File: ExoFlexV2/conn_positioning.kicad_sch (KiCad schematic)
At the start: 39 parts

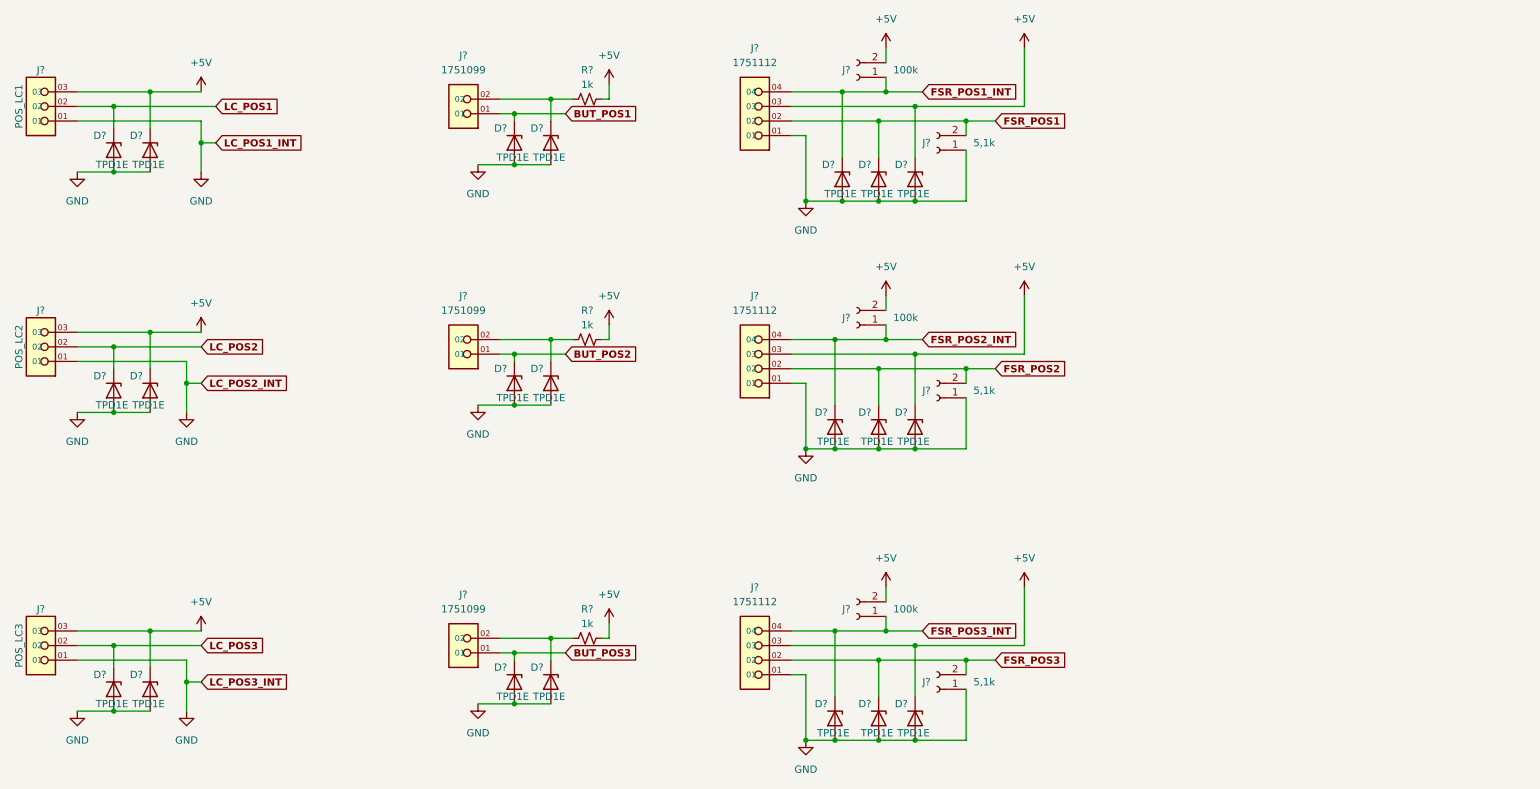
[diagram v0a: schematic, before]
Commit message: Mise à jour signaux STM
- Condo de découplage
- Signaux supplémentaire pour le STM
- Page GND sera pour Multiplexeur
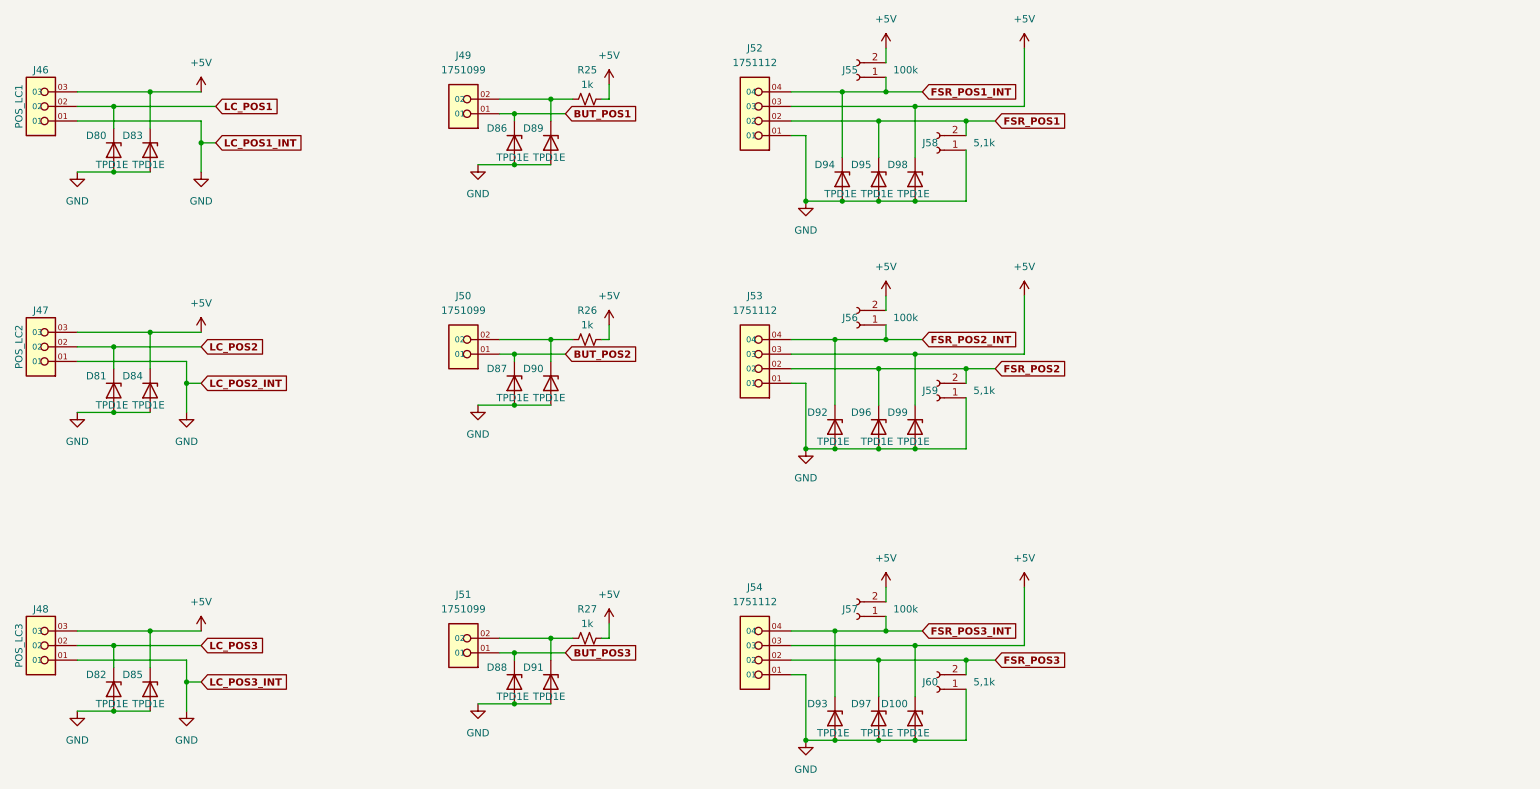
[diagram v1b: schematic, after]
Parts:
- gave numbers to parts that had none: 39

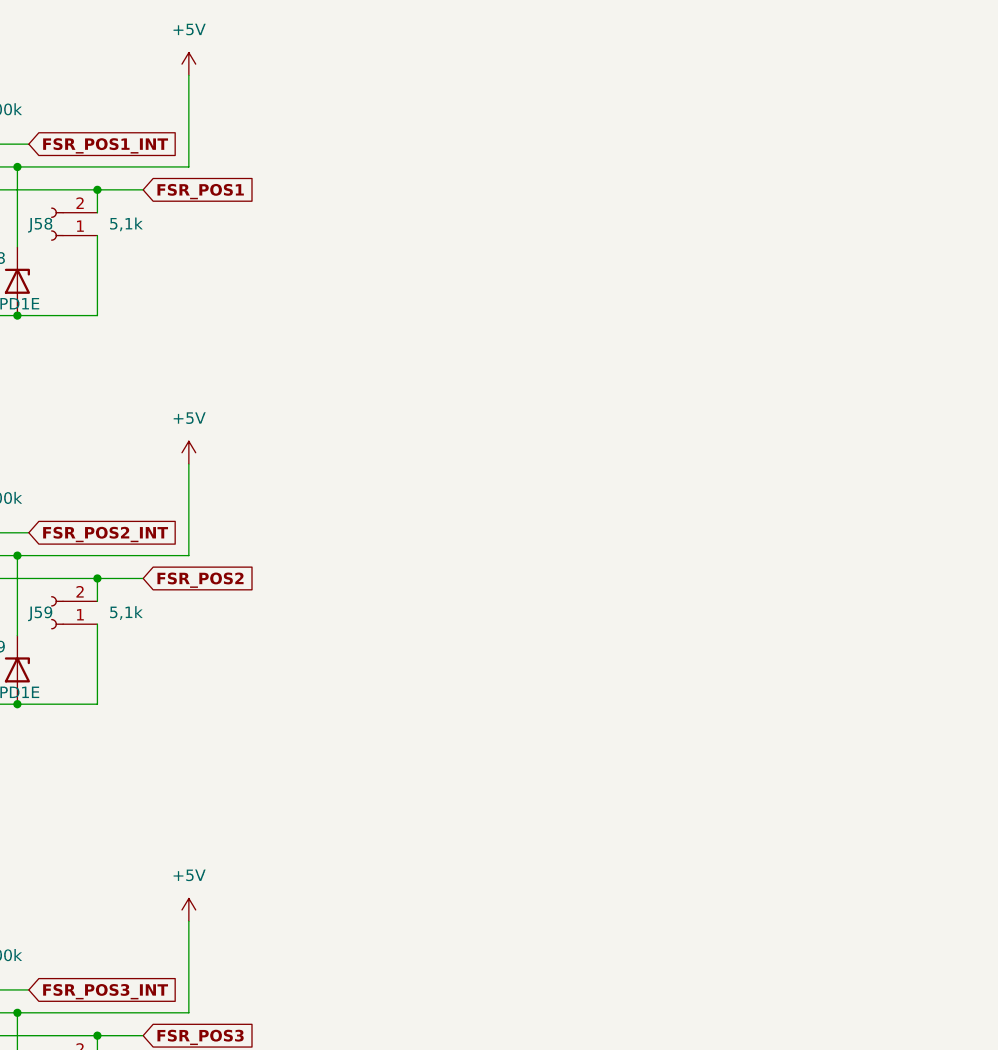
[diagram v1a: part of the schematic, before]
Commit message: Finalisation 1
- Ajout de pages pour la gestion des signaux négatif
- Modification des pages de torque et amplitude
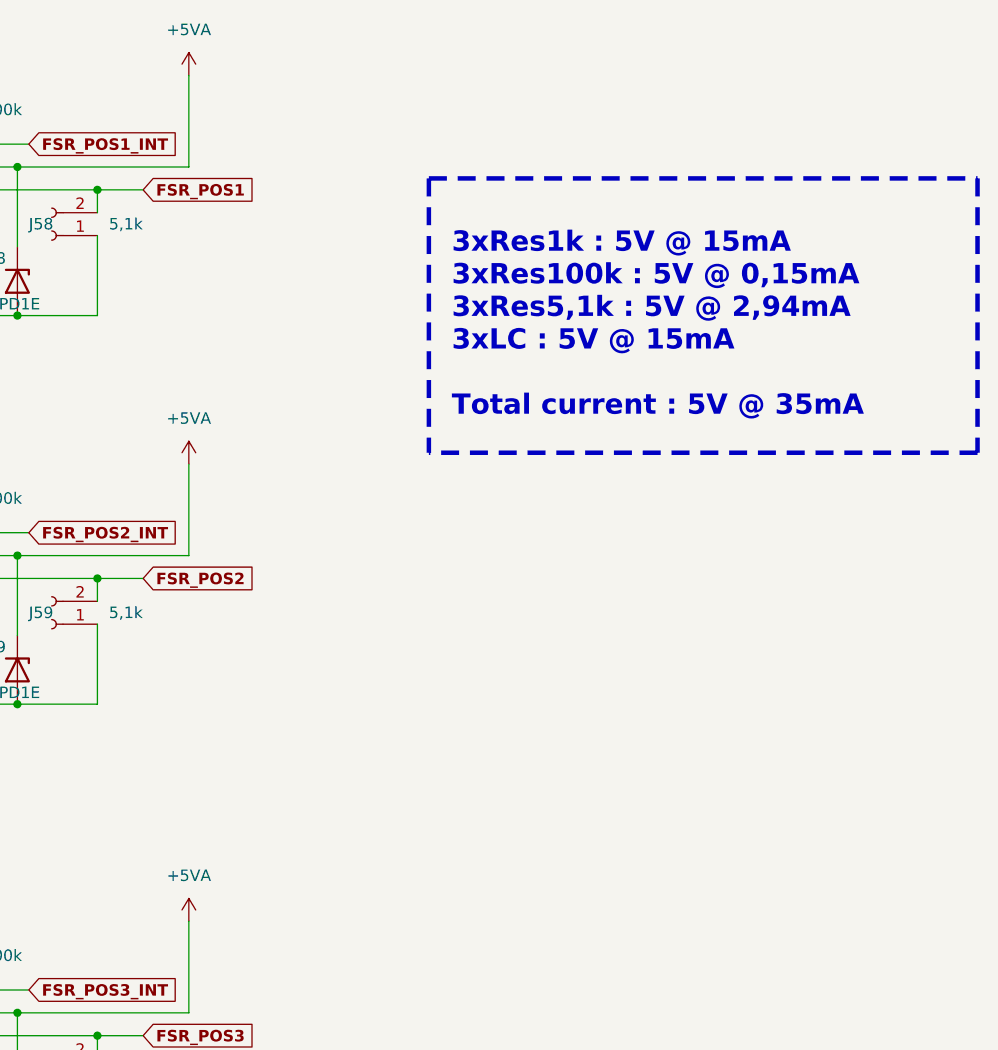
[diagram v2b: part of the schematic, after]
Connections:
- net +5V: no longer D100.1 (K), D98.1 (K), D99.1 (K), J52.03, J53.03, J54.03
- new net +5VA: D100.1 (K), D98.1 (K), D99.1 (K), J52.03, J53.03, J54.03
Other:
- note added: "3xRes1k : 5V @ 15mA 3xRes100k : 5V @ 0,15mA 3xRes5,1k : 5V @ 2,94mA 3xLC : 5V @ 15mA Total current : 5V @ 35mA"
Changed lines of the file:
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@@
     (stroke (width 0) (type default) (color 0 0 0 0))
+  )
+  (polyline (pts (xy 222.25 33.02) (xy 283.21 33.02))
+    (stroke (width 0.5) (type dash) (color 255 148 44 1))
   )
   (wire (pts (xy 170.18 77.47) (xy 185.42 77.47))
@@
     (stroke (width 0) (type default) (color 0 0 0 0))
   )
+  (polyline (pts (xy 283.21 33.02) (xy 283.21 63.5))
+    (stroke (width 0.5) (type dash) (color 255 148 44 1))
+  )
   (wire (pts (xy 36.83 125.73) (xy 52.07 125.73))
     (stroke (width 0) (type default) (color 0 0 0 0))
@@
     (stroke (width 0) (type default) (color 0 0 0 0))
   )
+  (polyline (pts (xy 283.21 63.5) (xy 222.25 63.5))
+    (stroke (width 0.5) (type dash) (color 255 148 44 1))
+  )
   (wire (pts (xy 171.45 72.39) (xy 162.56 72.39))
     (stroke (width 0) (type default) (color 0 0 0 0))
@@
     (stroke (width 0) (type default) (color 0 0 0 0))
   )
+  (polyline (pts (xy 222.25 33.02) (xy 222.25 63.5))
+    (stroke (width 0.5) (type dash) (color 255 148 44 1))
+  )
   (wire (pts (xy 162.56 123.19) (xy 162.56 134.62))
     (stroke (width 0) (type default) (color 0 0 0 0))
@@
   (wire (pts (xy 157.48 48.26) (xy 163.83 48.26))
     (stroke (width 0) (type default) (color 0 0 0 0))
+  )
+  (text "3xRes1k : 5V @ 15mA\n3xRes100k : 5V @ 0,15mA\n3xRes5,1k : 5V @ 2,94mA\n3xLC : 5V @ 15mA\n\nTotal current : 5V @ 35mA"
+    (at 224.79 59.69 0)
+    (effects (font (size 2.25 2.25) (thickness 0.5) bold) (justify left bottom))
   )
   (global_label "LC_POS1_INT" (shape input) (at 54.61 38.1 0) (fields_autoplaced)
@@
     (pin "02")
   )
-  (symbol (lib_id "power:+5V") (at 195.58 115.57 0) (unit 1)
-    (in_bom yes) (on_board yes) (fields_autoplaced)
-    (property "Reference" "#PWR0116" (id 0) (at 195.58 119.38 0)
-      (effects (font (size 1.27 1.27)) hide)
-    )
-    (property "Value" "+5V" (id 1) (at 195.58 110.49 0))
-    (property "Footprint" "" (id 2) (at 195.58 115.57 0)
-      (effects (font (size 1.27 1.27)) hide)
-    )
-    (property "Datasheet" "" (id 3) (at 195.58 115.57 0)
-      (effects (font (size 1.27 1.27)) hide)
-    )
-    (pin "1")
-  )
   (symbol (lib_id "Device:D_Zener") (at 113.03 132.08 270) (unit 1)
     (in_bom yes) (on_board yes)
@@
     (pin "1")
     (pin "2")
-  )
-  (symbol (lib_id "power:+5V") (at 195.58 64.77 0) (unit 1)
-    (in_bom yes) (on_board yes) (fields_autoplaced)
-    (property "Reference" "#PWR0115" (id 0) (at 195.58 68.58 0)
-      (effects (font (size 1.27 1.27)) hide)
-    )
-    (property "Value" "+5V" (id 1) (at 195.58 59.69 0))
-    (property "Footprint" "" (id 2) (at 195.58 64.77 0)
-      (effects (font (size 1.27 1.27)) hide)
-    )
-    (property "Datasheet" "" (id 3) (at 195.58 64.77 0)
-      (effects (font (size 1.27 1.27)) hide)
-    )
-    (pin "1")
   )
   (symbol (lib_id "SymLib:1751112") (at 144.78 125.73 180) (unit 1)
@@
     (pin "1")
   )
-  (symbol (lib_id "power:+5V") (at 195.58 21.59 0) (unit 1)
-    (in_bom yes) (on_board yes) (fields_autoplaced)
-    (property "Reference" "#PWR0114" (id 0) (at 195.58 25.4 0)
-      (effects (font (size 1.27 1.27)) hide)
-    )
-    (property "Value" "+5V" (id 1) (at 195.58 16.51 0))
-    (property "Footprint" "" (id 2) (at 195.58 21.59 0)
-      (effects (font (size 1.27 1.27)) hide)
-    )
-    (property "Datasheet" "" (id 3) (at 195.58 21.59 0)
+  (symbol (lib_id "power:+5VA") (at 195.58 115.57 0) (unit 1)
+    (in_bom yes) (on_board yes) (fields_autoplaced)
+    (property "Reference" "#PWR?" (id 0) (at 195.58 119.38 0)
+      (effects (font (size 1.27 1.27)) hide)
+    )
+    (property "Value" "+5VA" (id 1) (at 195.58 110.49 0))
+    (property "Footprint" "" (id 2) (at 195.58 115.57 0)
+      (effects (font (size 1.27 1.27)) hide)
+    )
+    (property "Datasheet" "" (id 3) (at 195.58 115.57 0)
       (effects (font (size 1.27 1.27)) hide)
     )
@@
     (pin "1")
   )
+  (symbol (lib_id "power:+5VA") (at 195.58 64.77 0) (unit 1)
+    (in_bom yes) (on_board yes) (fields_autoplaced)
+    (property "Reference" "#PWR?" (id 0) (at 195.58 68.58 0)
+      (effects (font (size 1.27 1.27)) hide)
+    )
+    (property "Value" "+5VA" (id 1) (at 195.58 59.69 0))
+    (property "Footprint" "" (id 2) (at 195.58 64.77 0)
+      (effects (font (size 1.27 1.27)) hide)
+    )
+    (property "Datasheet" "" (id 3) (at 195.58 64.77 0)
+      (effects (font (size 1.27 1.27)) hide)
+    )
+    (pin "1")
+  )
   (symbol (lib_id "Device:D_Zener") (at 43.18 39.37 270) (unit 1)
     (in_bom yes) (on_board yes)
@@
     (pin "2")
   )
+  (symbol (lib_id "power:+5VA") (at 195.58 21.59 0) (unit 1)
+    (in_bom yes) (on_board yes) (fields_autoplaced)
+    (property "Reference" "#PWR?" (id 0) (at 195.58 25.4 0)
+      (effects (font (size 1.27 1.27)) hide)
+    )
+    (property "Value" "+5VA" (id 1) (at 195.58 16.51 0))
+    (property "Footprint" "" (id 2) (at 195.58 21.59 0)
+      (effects (font (size 1.27 1.27)) hide)
+    )
+    (property "Datasheet" "" (id 3) (at 195.58 21.59 0)
+      (effects (font (size 1.27 1.27)) hide)
+    )
+    (pin "1")
+  )
 )
